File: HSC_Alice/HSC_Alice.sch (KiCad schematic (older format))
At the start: 213 parts, among them U2 Elite-C

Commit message: Numpad
Added Numpad Row and Col
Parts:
- D1, D10, D100, D101, D102, D103, D104, D105, D106, D11, D12, D13, D14, D15, D16, D17, D18, D19, D2, D20, D21, D22, D23, D24, D25, D26, D27, D28, D29, D3, D30, D31, D32, D33, D34, D35, D36, D37, D38, D39, D4, D40, D41, D42, D43, D44, D45, D46, D47, D48, D49, D5, D50, D51, D52, D53, D54, D55, D56, D57, D58, D59, D6, D60, D61, D62, D63, D64, D65, D66, D67, D68, D69, D7, D70, D71, D72, D73, D74, D75, D76, D77, D78, D79, D8, D80, D81, D82, D83, D84, D85, D86, D87, D88, D89, D9, D90, D91, D92, D93, D94, D95, D96, D97, D98, D99: renamed from D?; footprint (none) -> Diode_SMD:D_SOD-123
- MX1, MX10, MX100, MX102, MX103, MX105, MX106, MX11, MX12, MX13, MX15, MX16, MX17, MX19, MX2, MX20, MX21, MX22, MX23, MX24, MX25, MX26, MX29, MX3, MX31, MX32, MX33, MX34, MX35, MX37, MX38, MX39, MX4, MX40, MX41, MX43, MX44, MX45, MX46, MX47, MX49, MX5, MX50, MX51, MX52, MX53, MX54, MX55, MX56, MX57, MX58, MX59, MX60, MX61, MX62, MX63, MX64, MX65, MX66, MX67, MX68, MX69, MX7, MX70, MX71, MX73, MX74, MX75, MX76, MX77, MX79, MX8, MX80, MX81, MX82, MX83, MX85, MX86, MX87, MX88, MX89, MX9, MX91, MX92, MX93, MX94, MX97, MX98, MX99: renamed from MX?; footprint (none) -> MX_Alps_Hybrid:MX-1U-NoLED
- MX101: renamed from MX?; footprint (none) -> MX_Alps_Hybrid:MX-2.25U-NoLED
- MX104, MX14, MX18, MX48, MX6: renamed from MX?; footprint (none) -> MX_Alps_Hybrid:MX-2U-NoLED
- MX27: renamed from MX?; footprint (none) -> MX_Alps_Hybrid:MX-1.5U-NoLED
- MX28, MX95: renamed from MX?; footprint (none) -> MX_Alps_Hybrid:MX-1.75U-NoLED
- MX30, MX36, MX42, MX78, MX84, MX90, MX96: renamed from MX?; footprint (none) -> MX_Alps_Hybrid:MX-1.25U-NoLED
- MX72: renamed from MX?; footprint (none) -> MX_Alps_Hybrid:MX-2.75U-NoLED
- U2: footprint (none) -> Keebio-Parts:Elite-C-castellated-29pin-holes
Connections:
- net labels added: Col0, Col1, Col10, Col11, Col12, Col13, Col14, Col15, Col16, Col17, Col2, Col3, Col4, Col5, Col6, Col7, Col8, Col9, Row0, Row1, Row2, Row3, Row4, Row5

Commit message: 1st angled col added
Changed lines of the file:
@@
 Text GLabel 2750 5200 0    50   Input ~ 0
 Row5
+Text GLabel 775  900  0    50   Input ~ 0
+Col0
+Text GLabel 775  1000 0    50   Input ~ 0
+Col1
+Text GLabel 775  1300 0    50   Input ~ 0
+Col2
+Text GLabel 775  1400 0    50   Input ~ 0
+Col3
+Text GLabel 775  1500 0    50   Input ~ 0
+Col4
+Text GLabel 775  1600 0    50   Input ~ 0
+Col5
+Text GLabel 775  1700 0    50   Input ~ 0
+Col6
+Text GLabel 775  1800 0    50   Input ~ 0
+Row0
+Text GLabel 775  1900 0    50   Input ~ 0
+Row1
+Text GLabel 775  2000 0    50   Input ~ 0
+Row2
+Text GLabel 1275 2400 3    50   Input ~ 0
+Row3
+Text GLabel 1375 2400 3    50   Input ~ 0
+Row4
+Text GLabel 1475 2400 3    50   Input ~ 0
+Row5
 $EndSCHEMATC

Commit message: Finished PCB
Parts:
- removed D100, D106: D_Small, Diode_SMD:D_SOD-123, symbol Device:D_Small
- removed MX100: \\, MX_Alps_Hybrid:MX-1U-NoLED, symbol MX_Alps_Hybrid:MX-NoLED
- removed MX106: ENTER, MX_Alps_Hybrid:MX-1U-NoLED, symbol MX_Alps_Hybrid:MX-NoLED
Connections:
- wire segments 212 -> 208
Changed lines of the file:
@@
-$EndComp
-$Comp
-L MX_Alps_Hybrid:MX-NoLED MX100
-U 1 1 60DA7E97
-P 11100 3350
-F 0 "MX100" H 11133 3573 60  0000 C CNN
-F 1 "\\" H 11133 3499 20  0000 C CNN
-F 2 "MX_Alps_Hybrid:MX-1U-NoLED" H 10475 3325 60  0001 C CNN
-F 3 "" H 10475 3325 60  0001 C CNN
-	1    11100 3350
-	1    0    0    -1
-$EndComp
-$Comp
-L Device:D_Small D100
-U 1 1 60DA7E9D
-P 11050 3600
-F 0 "D100" V 11096 3530 50  0000 R CNN
-F 1 "D_Small" V 11005 3530 50  0000 R CNN
-F 2 "Diode_SMD:D_SOD-123" V 11050 3600 50  0001 C CNN
-F 3 "~" V 11050 3600 50  0001 C CNN
-	1    11050 3600
-	0    -1   -1   0
-$EndComp
-$Comp
-L MX_Alps_Hybrid:MX-NoLED MX106
-U 1 1 60DA7EA3
-P 11600 3350
-F 0 "MX106" H 11633 3573 60  0000 C CNN
-F 1 "ENTER" H 11633 3499 20  0000 C CNN
-F 2 "MX_Alps_Hybrid:MX-1U-NoLED" H 10975 3325 60  0001 C CNN
-F 3 "" H 10975 3325 60  0001 C CNN
-	1    11600 3350
-	1    0    0    -1
-$EndComp
-$Comp
-L Device:D_Small D106
-U 1 1 60DA7EA9
-P 11550 3600
-F 0 "D106" V 11596 3530 50  0000 R CNN
-F 1 "D_Small" V 11505 3530 50  0000 R CNN
-F 2 "Diode_SMD:D_SOD-123" V 11550 3600 50  0001 C CNN
-F 3 "~" V 11550 3600 50  0001 C CNN
-	1    11550 3600
-	0    -1   -1   0
 $EndComp
 $Comp
@@
 Wire Wire Line
 	11250 1800 11250 2550
-Connection ~ 11250 2550
-Wire Wire Line
-	11250 2550 11250 3300
-Connection ~ 11250 3300
-Wire Wire Line
-	11250 3300 11250 4050
-Connection ~ 11250 4050
 Wire Wire Line
 	11250 4050 11250 4800
@@
 Wire Wire Line
 	11750 1800 11750 2550
-Connection ~ 11750 2550
-Wire Wire Line
-	11750 2550 11750 3300
 Wire Wire Line
 	2750 1450 3050 1450
@@
 Wire Wire Line
 	10050 3700 10550 3700
-Connection ~ 10550 3700
-Wire Wire Line
-	10550 3700 11050 3700
-Connection ~ 11050 3700
-Wire Wire Line
-	11050 3700 11550 3700
 Wire Wire Line
 	2750 4450 3050 4450
@@
 Text GLabel 1475 2400 3    50   Input ~ 0
 Row5
+Text GLabel 1575 2400 3    50   Input ~ 0
+Col7
+Text GLabel 1675 2400 3    50   Input ~ 0
+Col8
+Text GLabel 2175 2000 2    50   Input ~ 0
+Col9
+Text GLabel 2175 1900 2    50   Input ~ 0
+Col10
+Text GLabel 2175 1800 2    50   Input ~ 0
+Col11
+Text GLabel 2175 1700 2    50   Input ~ 0
+Col12
+Text GLabel 2175 1600 2    50   Input ~ 0
+Col13
+Text GLabel 2175 1500 2    50   Input ~ 0
+Col14
+Text GLabel 2175 1400 2    50   Input ~ 0
+Col15
+Text GLabel 2175 1300 2    50   Input ~ 0
+Col16
+Text GLabel 2175 900  2    50   Input ~ 0
+Col17
+Wire Wire Line
+	11250 2550 11250 4050
+Connection ~ 11250 2550
+Connection ~ 11250 4050
 $EndSCHEMATC

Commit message: Microcontroller
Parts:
- removed U2: Elite-C, Keebio-Parts:Elite-C-castellated-29pin-holes, symbol keebio:Elite-C
- added C1, C2: 22pF, Capacitor_SMD:C_0805_2012Metric, symbol Device:C_Small
- added C3, C4, C6: 0.1uF, Capacitor_SMD:C_0805_2012Metric, symbol Device:C_Small
- added C5: 1uF, Capacitor_SMD:C_0805_2012Metric, symbol Device:C_Small
- added C7: 10uF, Capacitor_SMD:C_0805_2012Metric, symbol Device:C_Small
- added F1: 500mA, Fuse:Fuse_1206_3216Metric, symbol Device:Polyfuse_Small
- added R1, R2: 22, Resistor_SMD:R_0805_2012Metric, symbol Device:R_Small
- added R3, R4: 10k, Resistor_SMD:R_0805_2012Metric, symbol Device:R_Small
- added SW1: SW_Push, random-keyboard-parts:SKQG-1155865, symbol Switch:SW_Push
- added U1: ATmega32U4-AU, Package_QFP:TQFP-44_10x10mm_P0.8mm, symbol MCU_Microchip_ATmega:ATmega32U4-AU
- added USB1: Molex-0548190589, random-keyboard-parts:Molex-0548190589, symbol random-keyboard-parts:Molex-0548190589
- added Y1: Crystal_GND24_Small, Crystal:Crystal_SMD_3225-4Pin_3.2x2.5mm, symbol Device:Crystal_GND24_Small
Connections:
- net labels added: +5V, D+, D-, GND, VCC
- wire segments 208 -> 256

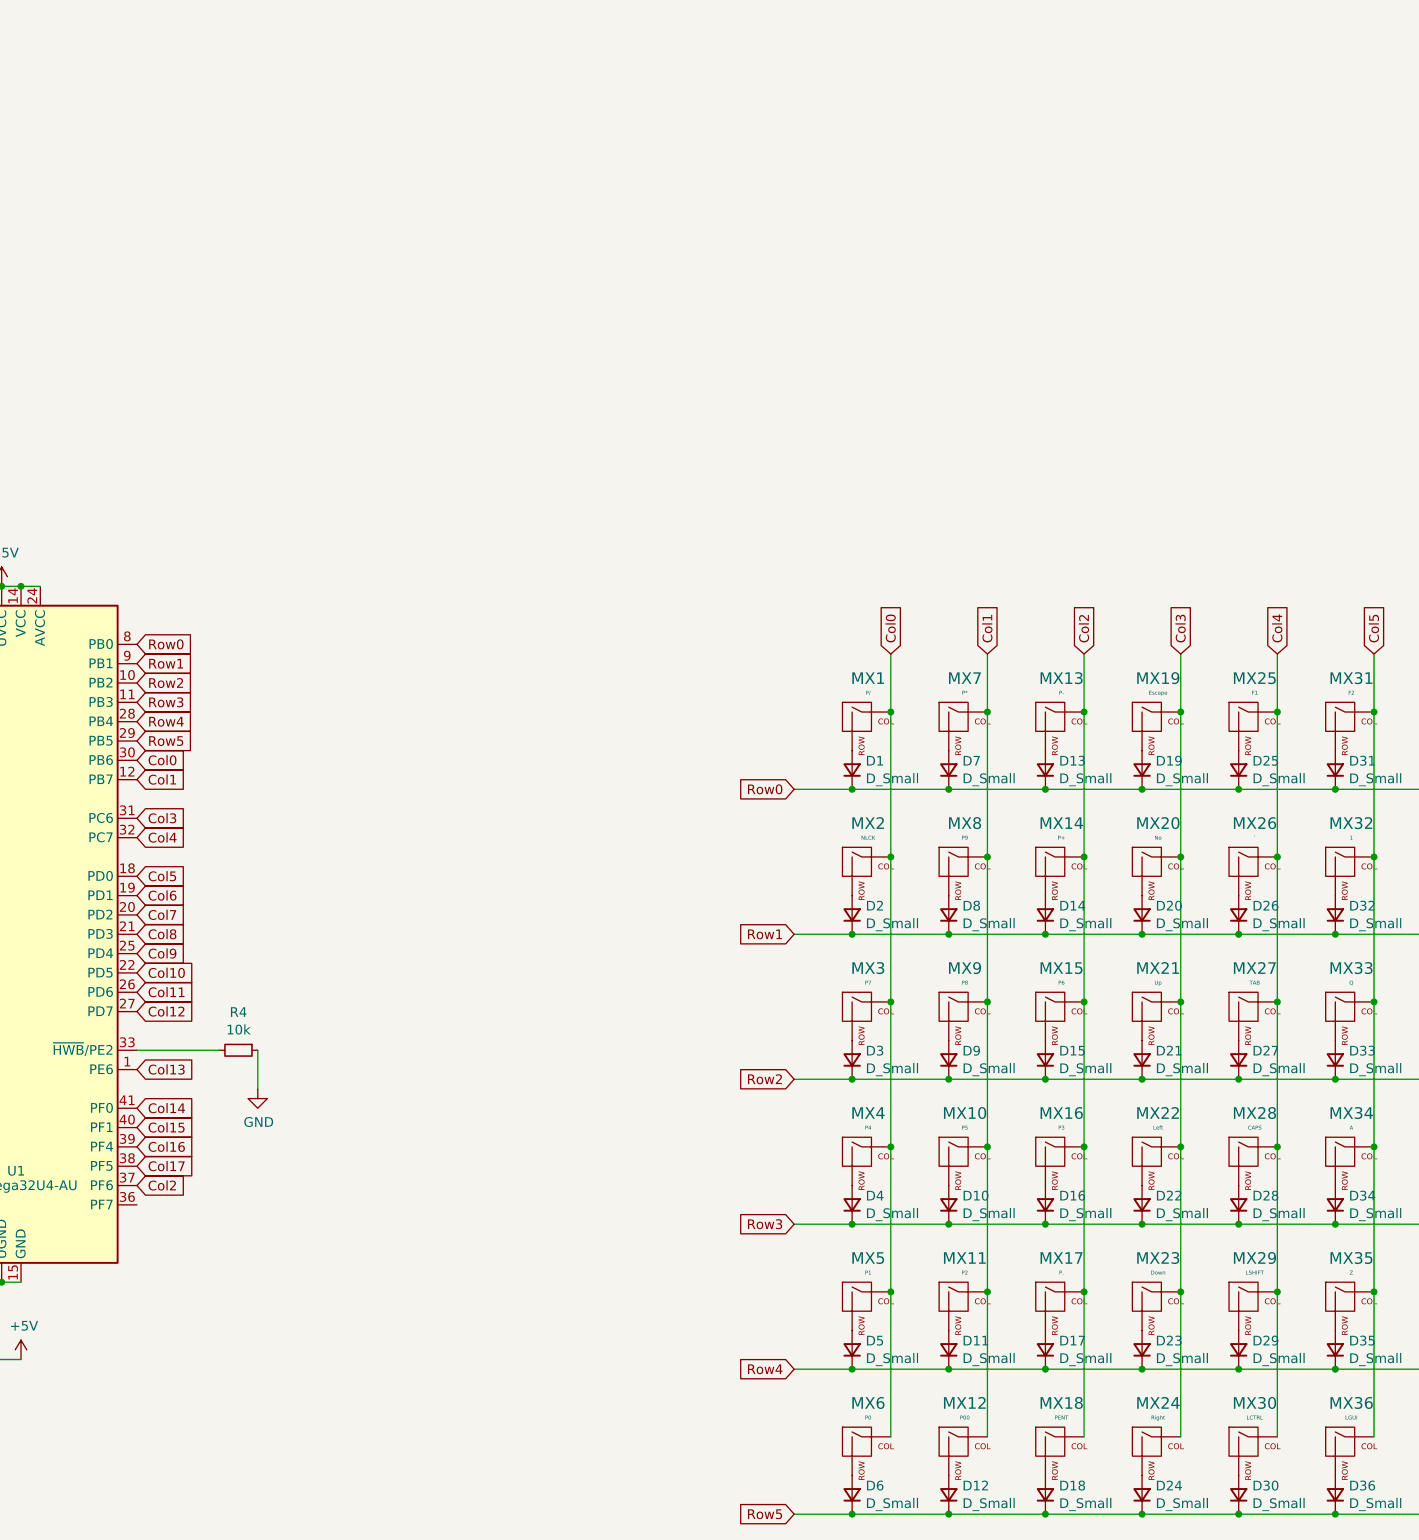
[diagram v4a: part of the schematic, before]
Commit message: Re-haul Schematics
Placed all SMD components on backside of PCB
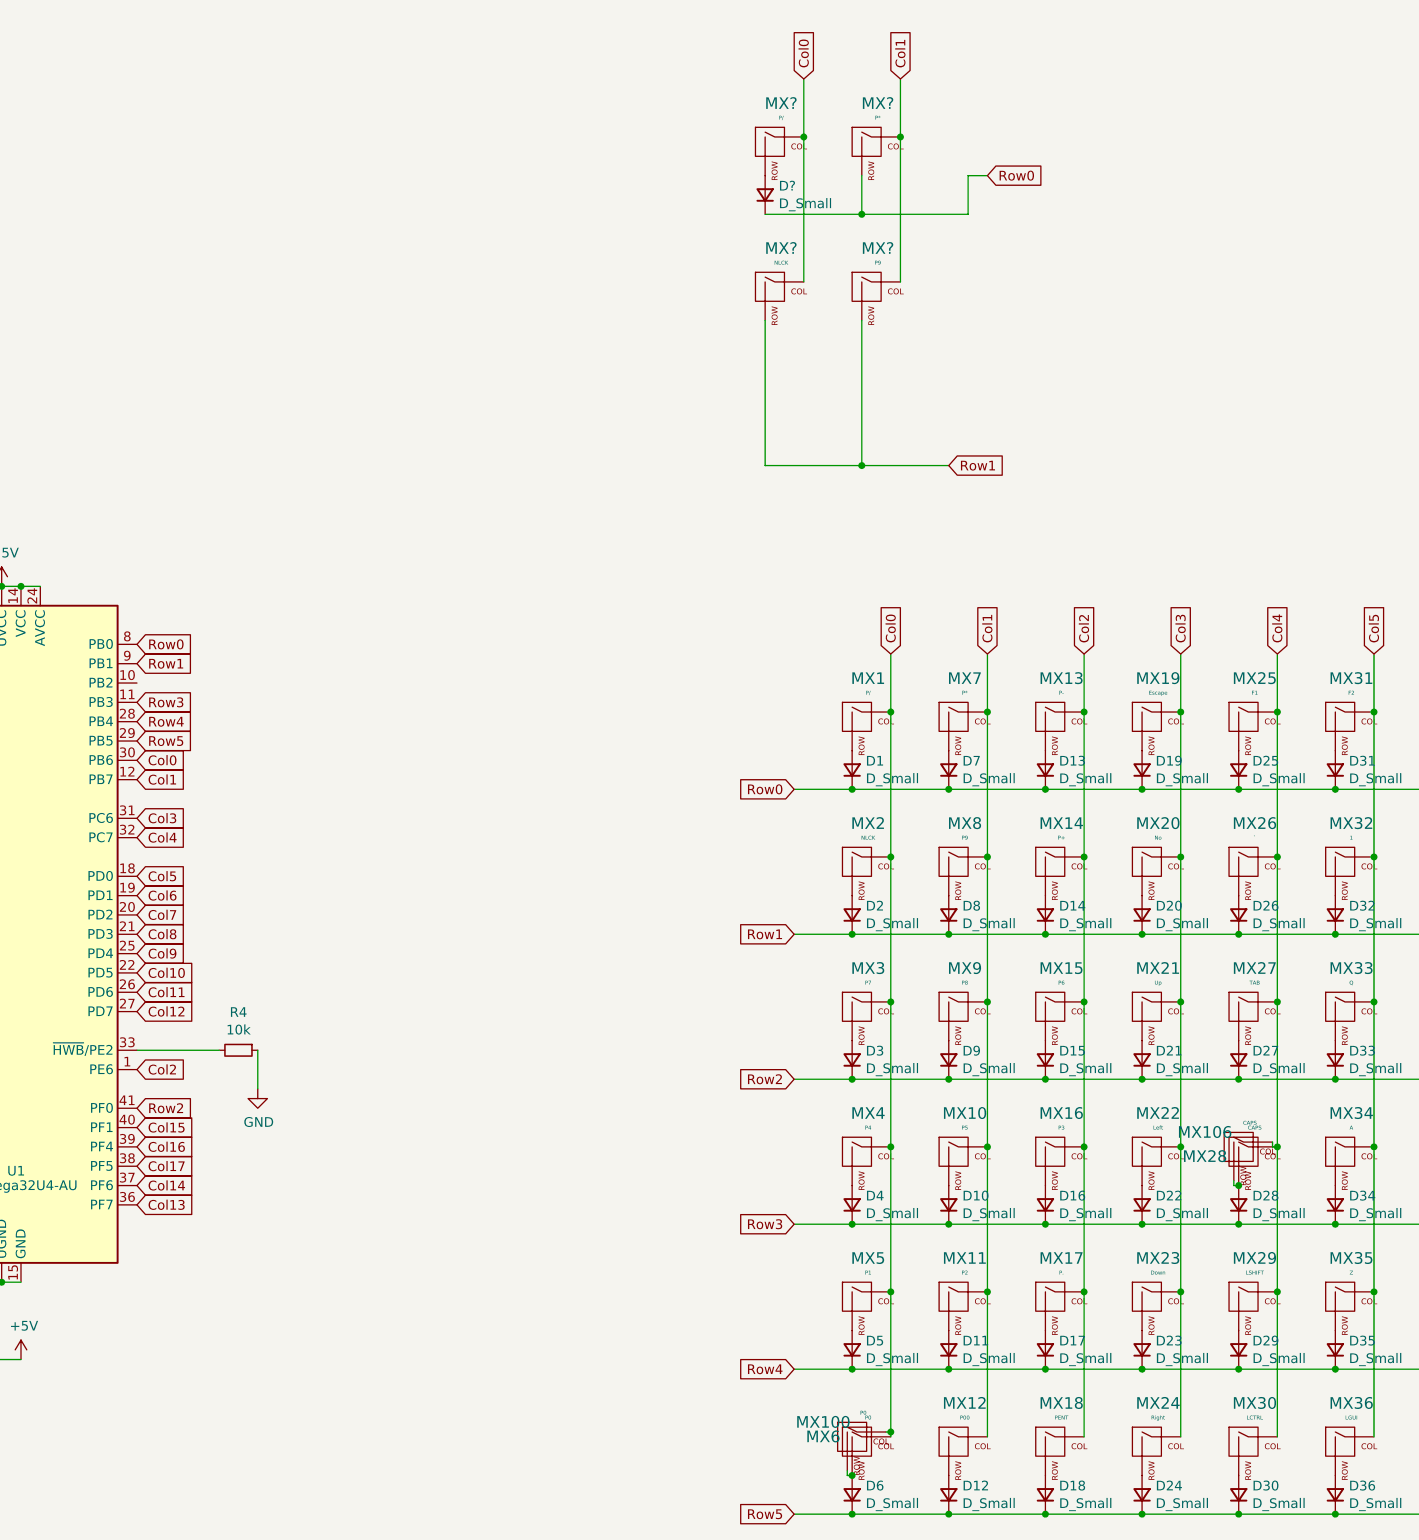
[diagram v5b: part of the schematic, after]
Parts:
- added D?: D_Small, symbol Device:D_Small
- added MX100: P0, MX_Alps_Hybrid:MX-2U-ReversedStabilizers-NoLED, symbol MX_Alps_Hybrid:MX-NoLED
- added MX106: CAPS, MX_Alps_Hybrid:MX-1.25U-NoLED, symbol MX_Alps_Hybrid:MX-NoLED
- added MX?: P/, MX_Alps_Hybrid:MX-1U-NoLED, symbol MX_Alps_Hybrid:MX-NoLED
- added MX?: P*, MX_Alps_Hybrid:MX-1U-NoLED, symbol MX_Alps_Hybrid:MX-NoLED
- added MX?: NLCK, MX_Alps_Hybrid:MX-1U-NoLED, symbol MX_Alps_Hybrid:MX-NoLED
- added MX?: P9, MX_Alps_Hybrid:MX-1U-NoLED, symbol MX_Alps_Hybrid:MX-NoLED
- MX105: footprint MX_Alps_Hybrid:MX-1U-NoLED -> MX_Alps_Hybrid:MX-1.5U-NoLED
- MX48: footprint MX_Alps_Hybrid:MX-2U-NoLED -> MX_Alps_Hybrid:MX-2.75U-ReversedStabilizers-NoLED
- MX6: footprint MX_Alps_Hybrid:MX-2U-NoLED -> MX_Alps_Hybrid:MX-1U-NoLED
- MX72: footprint MX_Alps_Hybrid:MX-2.75U-NoLED -> MX_Alps_Hybrid:MX-2.75U-ReversedStabilizers-NoLED
- MX95: footprint MX_Alps_Hybrid:MX-1.75U-NoLED -> MX_Alps_Hybrid:MX-2.25U-NoLED
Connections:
- net Col0: now also MX100.1 (COL), MX?.1 (COL), MX?.1 (COL)
- net Col1: now also MX?.1 (COL), MX?.1 (COL)
- net Col13: now also U1.36 (PF7); no longer U1.1 (PE6)
- net Col14: now also U1.37 (PF6); no longer U1.41 (PF0)
- net Col2: now also U1.1 (PE6); no longer U1.37 (PF6)
- net Col4: now also MX106.1 (COL)
- net Row0: now also D?.1 (K), MX?.2 (ROW)
- net Row1: now also MX?.2 (ROW), MX?.2 (ROW)
- net Row2: now also U1.41 (PF0); no longer U1.10 (PB2)
- net at D28.2 (A), MX28.2 (ROW): now also MX106.2 (ROW)
- net at D6.2 (A), MX6.2 (ROW): now also MX100.2 (ROW)
- new net: D?.2 (A), MX?.2 (ROW)
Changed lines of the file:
@@
 F 0 "MX105" H 11633 2823 60  0000 C CNN
 F 1 "\\" H 11633 2749 20  0000 C CNN
-F 2 "MX_Alps_Hybrid:MX-1U-NoLED" H 10975 2575 60  0001 C CNN
+F 2 "MX_Alps_Hybrid:MX-1.5U-NoLED" H 10975 2575 60  0001 C CNN
 F 3 "" H 10975 2575 60  0001 C CNN
 	1    11600 2600
@@
 U 1 1 60DA7E07
 P 5100 3350
-F 0 "MX28" H 5133 3573 60  0000 C CNN
+F 0 "MX28" H 4875 3350 60  0000 C CNN
 F 1 "CAPS" H 5133 3499 20  0000 C CNN
 F 2 "MX_Alps_Hybrid:MX-1.75U-NoLED" H 4475 3325 60  0001 C CNN
@@
 F 0 "MX95" H 10633 4323 60  0000 C CNN
 F 1 "RSHIFT" H 10633 4249 20  0000 C CNN
-F 2 "MX_Alps_Hybrid:MX-1.75U-NoLED" H 9975 4075 60  0001 C CNN
+F 2 "MX_Alps_Hybrid:MX-2.25U-NoLED" H 9975 4075 60  0001 C CNN
 F 3 "" H 9975 4075 60  0001 C CNN
 	1    10600 4100
@@
 U 1 1 60DE3351
 P 3100 4850
-F 0 "MX6" H 3133 5073 60  0000 C CNN
+F 0 "MX6" H 2900 4900 60  0000 C CNN
 F 1 "P0" H 3133 4999 20  0000 C CNN
-F 2 "MX_Alps_Hybrid:MX-2U-NoLED" H 2475 4825 60  0001 C CNN
+F 2 "MX_Alps_Hybrid:MX-1U-NoLED" H 2475 4825 60  0001 C CNN
 F 3 "" H 2475 4825 60  0001 C CNN
 	1    3100 4850
@@
 F 0 "MX48" H 6633 5073 60  0000 C CNN
 F 1 "SPACE" H 6633 4999 20  0000 C CNN
-F 2 "MX_Alps_Hybrid:MX-2U-NoLED" H 5975 4825 60  0001 C CNN
+F 2 "MX_Alps_Hybrid:MX-2.75U-ReversedStabilizers-NoLED" H 5975 4825 60  0001 C CNN
 F 3 "" H 5975 4825 60  0001 C CNN
 	1    6600 4850
@@
 F 0 "MX72" H 8633 5073 60  0000 C CNN
 F 1 "SPACE" H 8633 4999 20  0000 C CNN
-F 2 "MX_Alps_Hybrid:MX-2.75U-NoLED" H 7975 4825 60  0001 C CNN
+F 2 "MX_Alps_Hybrid:MX-2.75U-ReversedStabilizers-NoLED" H 7975 4825 60  0001 C CNN
 F 3 "" H 7975 4825 60  0001 C CNN
 	1    8600 4850
@@
 Connection ~ 3250 4050
 Wire Wire Line
-	3250 4050 3250 4800
+	3250 4050 3250 4775
 Wire Wire Line
 	3750 750  3750 1050
@@
 Text GLabel -650 800  2    50   Input ~ 0
 Row1
-Text GLabel -650 900  2    50   Input ~ 0
+Text GLabel -650 3100 2    50   Input ~ 0
 Row2
 Text GLabel -650 1000 2    50   Input ~ 0
@@
 Text GLabel -650 2600 2    50   Input ~ 0
 Col12
-Text GLabel -650 2900 2    50   Input ~ 0
+Text GLabel -650 3600 2    50   Input ~ 0
 Col13
-Text GLabel -650 3100 2    50   Input ~ 0
+Text GLabel -650 3500 2    50   Input ~ 0
 Col14
 Text GLabel -650 3200 2    50   Input ~ 0
@@
 Wire Wire Line
 	-25  2800 -25  3000
-Text GLabel -650 3500 2    50   Input ~ 0
+Text GLabel -650 2900 2    50   Input ~ 0
 Col2
 Wire Wire Line
 	-650 2800 -225 2800
+$Comp
+L MX_Alps_Hybrid:MX-NoLED MX100
+U 1 1 60E64824
+P 3075 4825
+F 0 "MX100" H 2900 4925 60  0000 C CNN
+F 1 "P0" H 3108 4974 20  0000 C CNN
+F 2 "MX_Alps_Hybrid:MX-2U-ReversedStabilizers-NoLED" H 2450 4800 60  0001 C CNN
+F 3 "" H 2450 4800 60  0001 C CNN
+	1    3075 4825
+	1    0    0    -1
+$EndComp
+Wire Wire Line
+	3225 4775 3250 4775
+Connection ~ 3250 4775
+Wire Wire Line
+	3250 4775 3250 4800
+Wire Wire Line
+	3025 4975 3025 5000
+Wire Wire Line
+	3025 5000 3050 5000
+Connection ~ 3050 5000
+Wire Wire Line
+	5025 3475 5025 3500
+Wire Wire Line
+	5025 3500 5050 3500
+Connection ~ 5050 3500
+Wire Wire Line
+	5225 3275 5225 3300
+Wire Wire Line
+	5225 3300 5250 3300
+$Comp
+L MX_Alps_Hybrid:MX-NoLED MX?
+U 1 1 6179FE4C
+P 2650 -1875
+F 0 "MX?" H 2683 -1652 60  0000 C CNN
+F 1 "P/" H 2683 -1726 20  0000 C CNN
+F 2 "MX_Alps_Hybrid:MX-1U-NoLED" H 2025 -1900 60  0001 C CNN
+F 3 "" H 2025 -1900 60  0001 C CNN
+	1    2650 -1875
+	1    0    0    -1
+$EndComp
+$Comp
+L MX_Alps_Hybrid:MX-NoLED MX?
+U 1 1 6179FE58
+P 3150 -1875
+F 0 "MX?" H 3183 -1652 60  0000 C CNN
+F 1 "P*" H 3183 -1726 20  0000 C CNN
+F 2 "MX_Alps_Hybrid:MX-1U-NoLED" H 2525 -1900 60  0001 C CNN
+F 3 "" H 2525 -1900 60  0001 C CNN
+	1    3150 -1875
+	1    0    0    -1
+$EndComp
+$Comp
+L MX_Alps_Hybrid:MX-NoLED MX?
+U 1 1 6179FE64
+P 2650 -1125
+F 0 "MX?" H 2683 -902 60  0000 C CNN
+F 1 "NLCK" H 2683 -976 20  0000 C CNN
+F 2 "MX_Alps_Hybrid:MX-1U-NoLED" H 2025 -1150 60  0001 C CNN
+F 3 "" H 2025 -1150 60  0001 C CNN
+	1    2650 -1125
+	1    0    0    -1
+$EndComp
+$Comp
+L MX_Alps_Hybrid:MX-NoLED MX?
+U 1 1 6179FE70
+P 3150 -1125
+F 0 "MX?" H 3183 -902 60  0000 C CNN
+F 1 "P9" H 3183 -976 20  0000 C CNN
+F 2 "MX_Alps_Hybrid:MX-1U-NoLED" H 2525 -1150 60  0001 C CNN
+F 3 "" H 2525 -1150 60  0001 C CNN
+	1    3150 -1125
+	1    0    0    -1
+$EndComp
+Wire Wire Line
+	2800 -2225 2800 -1925
+Wire Wire Line
+	2600 -975 2600 -225
+Wire Wire Line
+	3300 -2225 3300 -1925
+Wire Wire Line
+	3100 -975 3100 -225
+Text GLabel 2800 -2225 1    50   Input ~ 0
+Col0
+Text GLabel 3300 -2225 1    50   Input ~ 0
+Col1
+Text GLabel 3750 -1725 2    50   Input ~ 0
+Row0
+Wire Wire Line
+	2600 -225 3100 -225
+Connection ~ 3100 -225
+Wire Wire Line
+	3100 -225 3550 -225
+Text GLabel 3550 -225 2    50   Input ~ 0
+Row1
+Wire Wire Line
+	2800 -1925 2800 -1175
+Connection ~ 2800 -1925
+Wire Wire Line
+	3300 -1925 3300 -1175
+Connection ~ 3300 -1925
+$Comp
+L Device:D_Small D?
+U 1 1 618751ED
+P 2600 -1625
+F 0 "D?" V 2646 -1695 50  0000 R CNN
+F 1 "D_Small" V 2555 -1695 50  0000 R CNN
+F 2 "" V 2600 -1625 50  0001 C CNN
+F 3 "~" V 2600 -1625 50  0001 C CNN
+	1    2600 -1625
+	0    -1   -1   0
+$EndComp
+Wire Wire Line
+	2600 -1525 3100 -1525
+Wire Wire Line
+	3650 -1525 3650 -1725
+Wire Wire Line
+	3650 -1725 3750 -1725
+Wire Wire Line
+	3100 -1725 3100 -1525
+Connection ~ 3100 -1525
+Wire Wire Line
+	3100 -1525 3650 -1525
+$Comp
+L MX_Alps_Hybrid:MX-NoLED MX106
+U 1 1 61504233
+P 5075 3325
+F 0 "MX106" H 4875 3425 60  0000 C CNN
+F 1 "CAPS" H 5108 3474 20  0000 C CNN
+F 2 "MX_Alps_Hybrid:MX-1.25U-NoLED" H 4450 3300 60  0001 C CNN
+F 3 "" H 4450 3300 60  0001 C CNN
+	1    5075 3325
+	1    0    0    -1
+$EndComp
 $EndSCHEMATC
